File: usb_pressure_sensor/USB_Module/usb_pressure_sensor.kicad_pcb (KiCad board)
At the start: 2 copper layers, 45.7 x 27.9 mm, 21 parts, among them IC1 STM32F042F6P6, IC2 MCP1700, J1 CONN_02x09, J2 MODULE_BRIDGE, P1 SWD_TC, U1 MICRO_USB, U2 SN74LVC1GX04, U3 KSC341J:SWITCH, Y1 Crystal 32.768kHz

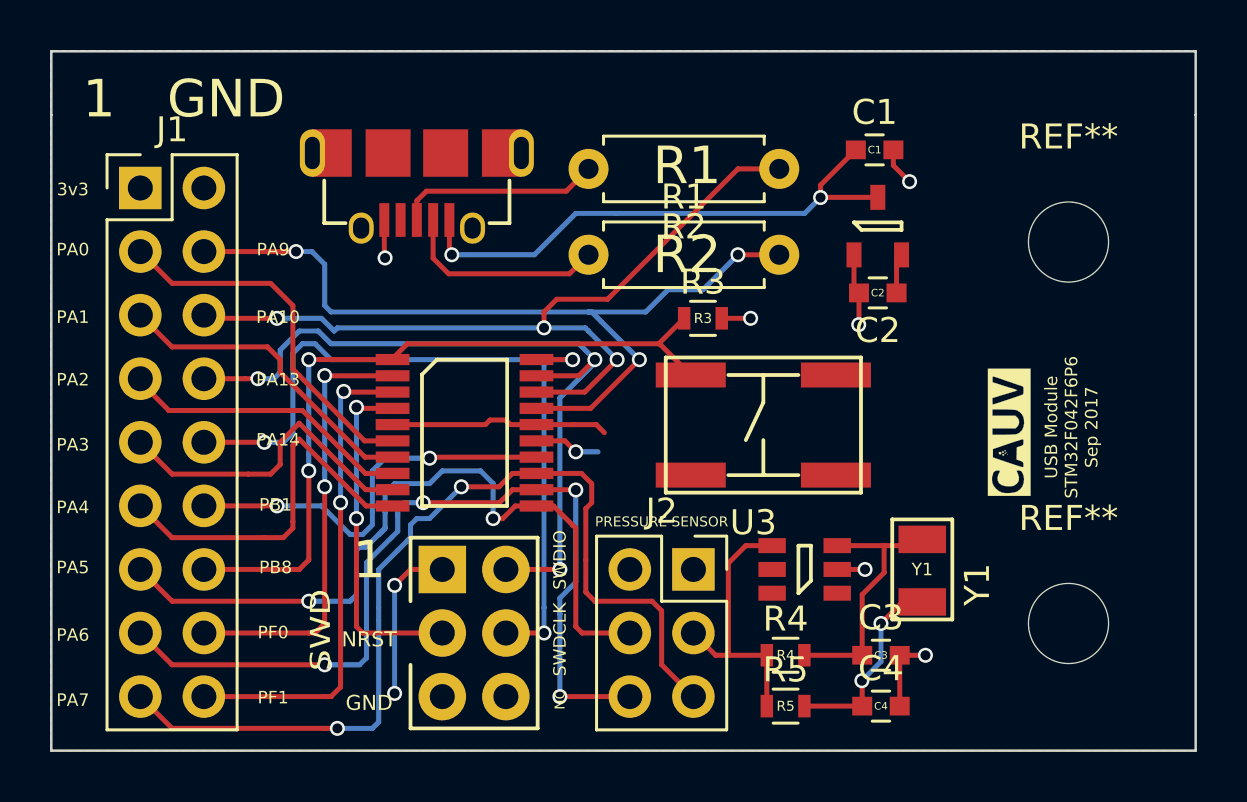
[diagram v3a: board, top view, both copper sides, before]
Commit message: Added LEDs to schematic
Removed cut since the cut needs to be aligned with the usb connector line so the sub connector hangs over the edge of the pcb
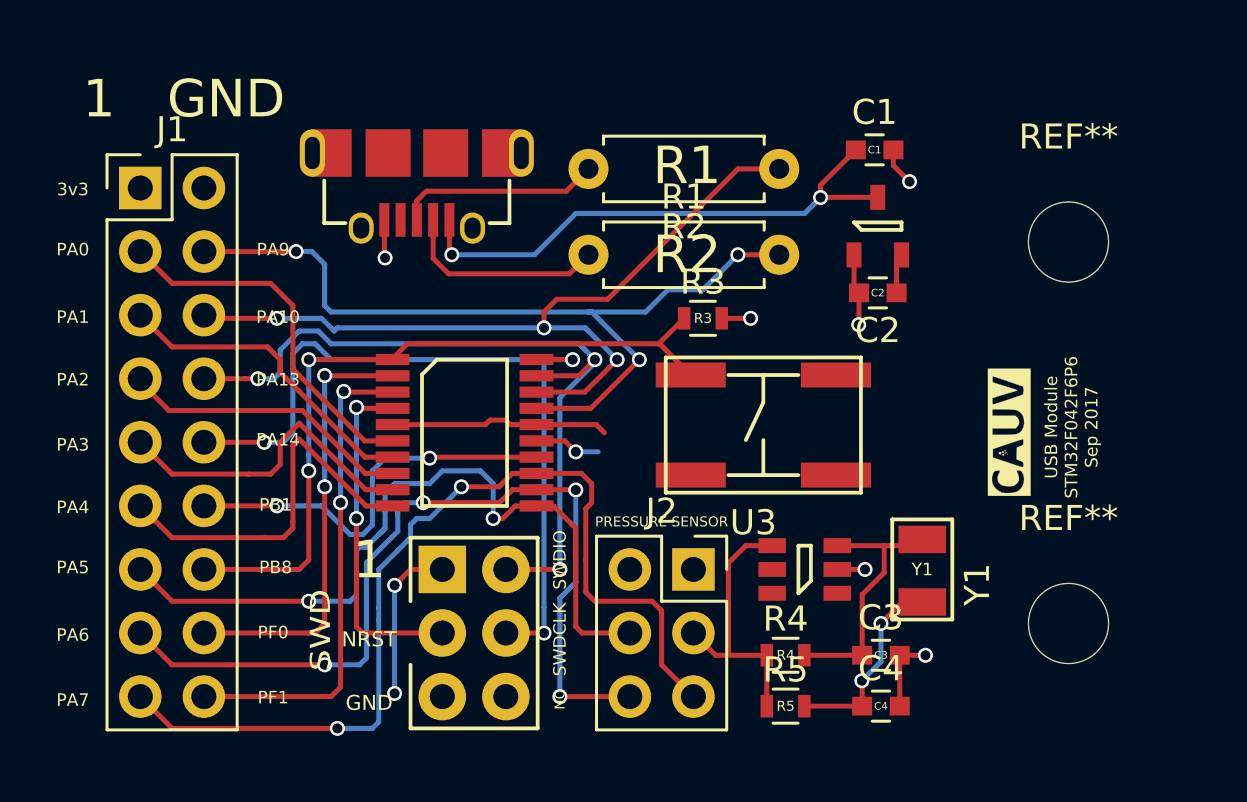
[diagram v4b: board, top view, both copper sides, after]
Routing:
- removed copper zone on F.Cu, net /3v3
- removed copper zone on B.Cu, net /GND
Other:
- board outline removed
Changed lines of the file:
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@@
-(kicad_pcb (version 4) (host pcbnew 4.0.6)
+(kicad_pcb (version 4) (host pcbnew 4.0.6-e0-6349~53~ubuntu16.04.1)
   (general
     (links 57)
-    (no_connects 0)
+    (no_connects 15)
     (area 116.704095 93.319 167.037143 123.209572)
     (thickness 1.6)
-    (drawings 37)
+    (drawings 31)
     (tracks 363)
     (zones 0)
@@
   (page A4)
   (layers
-    (0 F.Cu signal hide)
-    (31 B.Cu signal hide)
+    (0 F.Cu signal)
+    (31 B.Cu signal)
     (32 B.Adhes user hide)
     (33 F.Adhes user hide)
     (34 B.Paste user hide)
     (35 F.Paste user hide)
-    (36 B.SilkS user)
+    (36 B.SilkS user hide)
     (37 F.SilkS user)
     (38 B.Mask user hide)
@@
     (43 Eco2.User user hide)
     (44 Edge.Cuts user)
-    (45 Margin user)
-    (46 B.CrtYd user)
+    (45 Margin user hide)
+    (46 B.CrtYd user hide)
     (47 F.CrtYd user)
     (48 B.Fab user hide)
@@
     (effects (font (size 1.5 1.5) (thickness 0.3)))
   )
-  (gr_line (start 162.56 93.98) (end 162.56 96.52) (angle 90) (layer Edge.Cuts) (width 0.1))
-  (gr_line (start 116.84 93.98) (end 162.56 93.98) (angle 90) (layer Edge.Cuts) (width 0.1))
-  (gr_line (start 116.84 96.52) (end 116.84 93.98) (angle 90) (layer Edge.Cuts) (width 0.1))
-  (gr_line (start 162.56 121.92) (end 162.56 96.52) (angle 90) (layer Edge.Cuts) (width 0.1))
-  (gr_line (start 116.84 121.92) (end 162.56 121.92) (angle 90) (layer Edge.Cuts) (width 0.1))
-  (gr_line (start 116.84 96.52) (end 116.84 121.92) (angle 90) (layer Edge.Cuts) (width 0.1))
   (segment (start 150.483 97.917) (end 150.483 98.54) (width 0.2) (layer F.Cu) (net 1))
   (via (at 151.13 99.187) (size 0.6) (drill 0.4) (layers F.Cu B.Cu) (net 1))
@@
   (segment (start 129.286 117.221) (end 132.461 117.221) (width 0.2) (layer F.Cu) (net 9))
   (segment (start 129.032 116.967) (end 129.286 117.221) (width 0.2) (layer F.Cu) (net 9))
+  (segment (start 121.666 103.251) (end 120.396 101.981) (width 0.2) (layer F.Cu) (net 10))
   (segment (start 125.603 103.251) (end 121.666 103.251) (width 0.2) (layer F.Cu) (net 10))
   (segment (start 126.492 104.14) (end 125.603 103.251) (width 0.2) (layer F.Cu) (net 10))
@@
   (segment (start 126.746 106.934) (end 126.492 106.68) (width 0.2) (layer F.Cu) (net 10))
   (segment (start 126.492 106.68) (end 126.492 104.14) (width 0.2) (layer F.Cu) (net 10))
-  (segment (start 121.666 103.251) (end 120.396 101.981) (width 0.2) (layer F.Cu) (net 10))
   (segment (start 125.476 105.791) (end 121.666 105.791) (width 0.2) (layer F.Cu) (net 11))
   (segment (start 125.984 106.299) (end 125.476 105.791) (width 0.2) (layer F.Cu) (net 11))
@@
   (segment (start 125.984 106.807) (end 125.984 106.299) (width 0.2) (layer F.Cu) (net 11))
   (segment (start 121.666 105.791) (end 120.396 104.521) (width 0.2) (layer F.Cu) (net 11))
-  (segment (start 129.413 110.845) (end 129.387 110.845) (width 0.2) (layer F.Cu) (net 12))
   (segment (start 129.387 110.845) (end 126.873 108.331) (width 0.2) (layer F.Cu) (net 12))
   (segment (start 126.873 108.331) (end 124.968 108.331) (width 0.2) (layer F.Cu) (net 12))
+  (segment (start 124.968 108.331) (end 125.095 108.331) (width 0.2) (layer F.Cu) (net 12))
+  (segment (start 129.413 110.845) (end 129.387 110.845) (width 0.2) (layer F.Cu) (net 12))
+  (segment (start 129.413 110.845) (end 130.475 110.845) (width 0.2) (layer F.Cu) (net 12))
   (segment (start 120.396 107.061) (end 120.396 107.188) (width 0.2) (layer F.Cu) (net 12))
   (segment (start 120.396 107.188) (end 121.539 108.331) (width 0.2) (layer F.Cu) (net 12))
   (segment (start 121.539 108.331) (end 124.968 108.331) (width 0.2) (layer F.Cu) (net 12))
-  (segment (start 124.968 108.331) (end 125.095 108.331) (width 0.2) (layer F.Cu) (net 12))
-  (segment (start 129.413 110.845) (end 130.475 110.845) (width 0.2) (layer F.Cu) (net 12))
   (segment (start 124.714 110.871) (end 121.666 110.871) (width 0.2) (layer F.Cu) (net 13))
   (segment (start 125.984 109.601) (end 125.984 110.49) (width 0.2) (layer F.Cu) (net 13))
@@
   (segment (start 124.714 110.871) (end 125.603 110.871) (width 0.2) (layer F.Cu) (net 13))
   (segment (start 121.666 110.871) (end 120.396 109.601) (width 0.2) (layer F.Cu) (net 13))
-  (segment (start 125.349 113.411) (end 121.666 113.411) (width 0.2) (layer F.Cu) (net 14))
   (segment (start 126.492 112.776) (end 126.492 113.03) (width 0.2) (layer F.Cu) (net 14))
   (segment (start 126.619 109.601) (end 126.492 109.728) (width 0.2) (layer F.Cu) (net 14))
@@
   (segment (start 126.746 109.474) (end 126.619 109.601) (width 0.2) (layer F.Cu) (net 14))
   (segment (start 126.492 112.141) (end 126.492 112.776) (width 0.2) (layer F.Cu) (net 14))
+  (segment (start 126.492 113.03) (end 126.111 113.411) (width 0.2) (layer F.Cu) (net 14))
+  (segment (start 125.349 113.411) (end 121.666 113.411) (width 0.2) (layer F.Cu) (net 14))
   (segment (start 126.111 113.411) (end 125.349 113.411) (width 0.2) (layer F.Cu) (net 14))
-  (segment (start 126.492 113.03) (end 126.111 113.411) (width 0.2) (layer F.Cu) (net 14))
   (segment (start 121.666 113.411) (end 120.396 112.141) (width 0.2) (layer F.Cu) (net 14))
   (segment (start 137.795 115.189) (end 137.795 116.967) (width 0.2) (layer F.Cu) (net 15))
@@
   (segment (start 131.826 99.568) (end 137.414 99.568) (width 0.2) (layer F.Cu) (net 26))
   (segment (start 131.445 99.949) (end 131.826 99.568) (width 0.2) (layer F.Cu) (net 26))
-  (zone (net 3) (net_name /3v3) (layer F.Cu) (hatch edge 0.508)
-    (connect_pads (clearance 0.254))
-    (min_thickness 0.254)
-    (fill yes (arc_segments 16) (thermal_gap 0.508) (thermal_bridge_width 0.508))
-    (polygon
-      (pts
-        (xy 162.56 121.92) (xy 116.84 121.92) (xy 116.84 93.98) (xy 162.56 93.98)
-      )
-    )
-  )
-  (zone (net 1) (net_name /GND) (layer B.Cu) (hatch edge 0.508)
-    (connect_pads (clearance 0.254))
-    (min_thickness 0.254)
-    (fill yes (arc_segments 16) (thermal_gap 0.508) (thermal_bridge_width 0.508))
-    (polygon
-      (pts
-        (xy 162.56 121.92) (xy 116.84 121.92) (xy 116.84 93.98) (xy 162.56 93.98)
-      )
-    )
-  )
 )

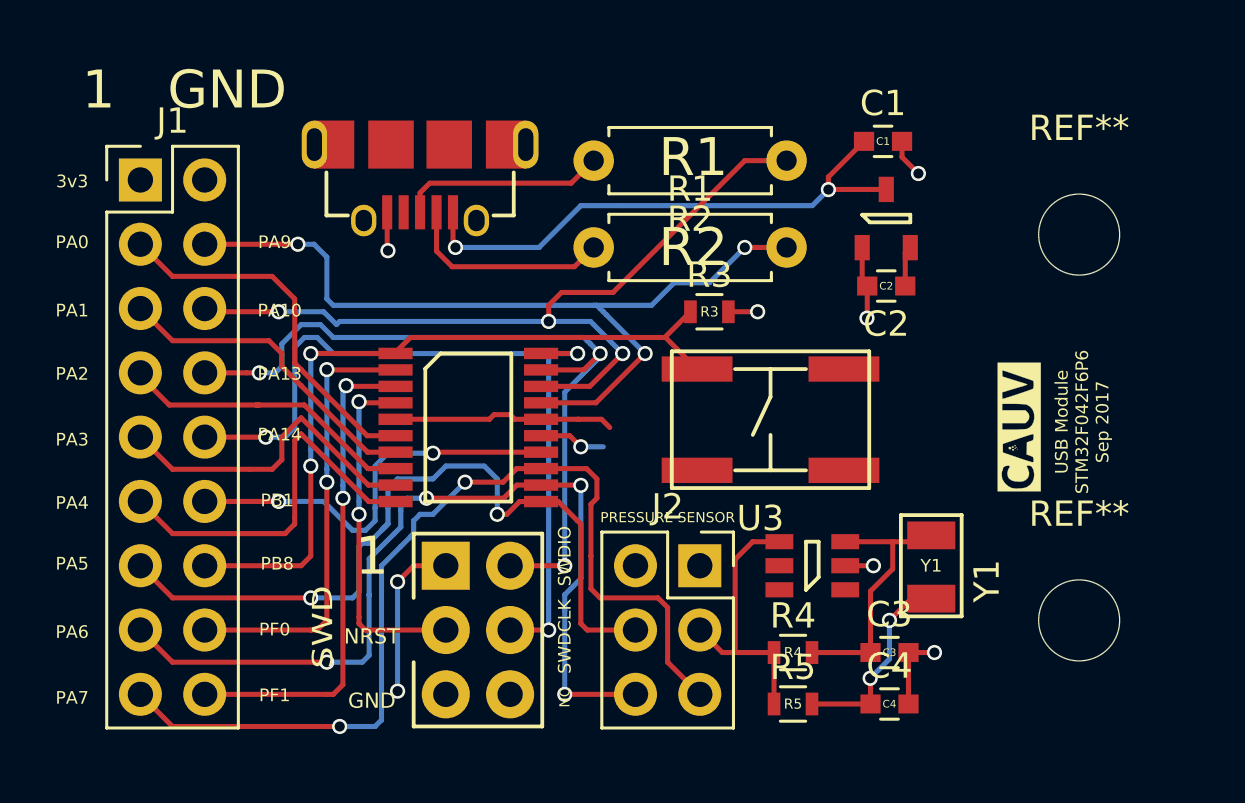
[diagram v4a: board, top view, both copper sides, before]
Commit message: added LEDs
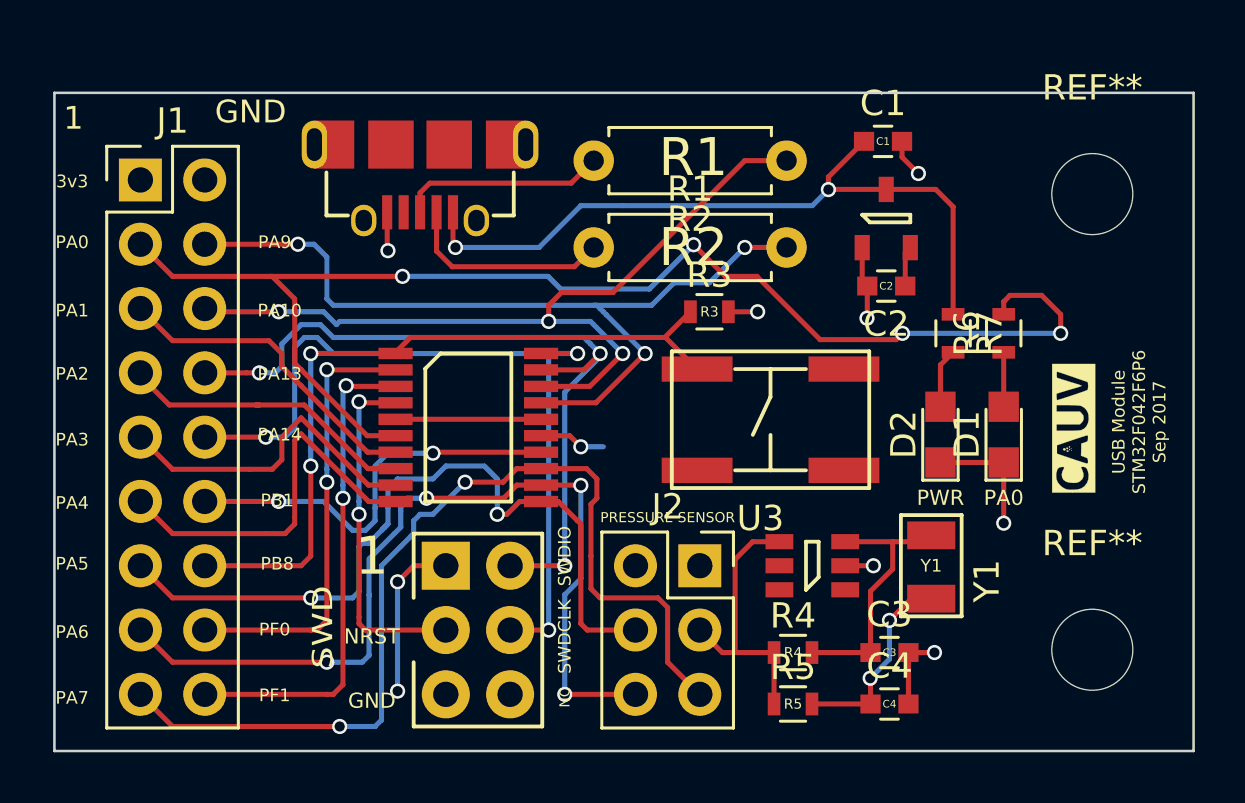
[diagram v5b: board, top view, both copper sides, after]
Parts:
- added D1: LED, LEDs:LED_0805, F.Cu at (154.5, 109.5)
- added D2: LED, LEDs:LED_0805, F.Cu at (152.0, 109.5)
- added R6: 1K, Resistors_SMD:R_0603, F.Cu at (154.5, 105.5)
- added R7: 1K, Resistors_SMD:R_0603, F.Cu at (152.5, 105.5)
- moved G*** 2.15 mm to (157.2, 109.2)
- moved REF** 1.68 mm to (158.0, 100.0)
- moved REF** 1.27 mm to (158.0, 118.0)
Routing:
- net /PA0: track 14.7 -> 52.5 mm, vias 0 -> 4
- net /5v: track 21.9 -> 29.1 mm
- net /GND: track 13.9 -> 18.8 mm, vias 7 -> 8
- net /3v3: track 17.0 -> 14.0 mm
- net Net-(D2-Pad2): track 0.00 -> 2.36 mm
- net Net-(D1-Pad2): track 0.00 -> 2.15 mm
- added copper zone on F.Cu, net /3v3
- added copper zone on B.Cu, net /GND
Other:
- board outline added: 45 x 26 mm
- board text added: "PWR"
